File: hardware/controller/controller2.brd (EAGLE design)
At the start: 65.7 x 33.2 mm, 15 parts

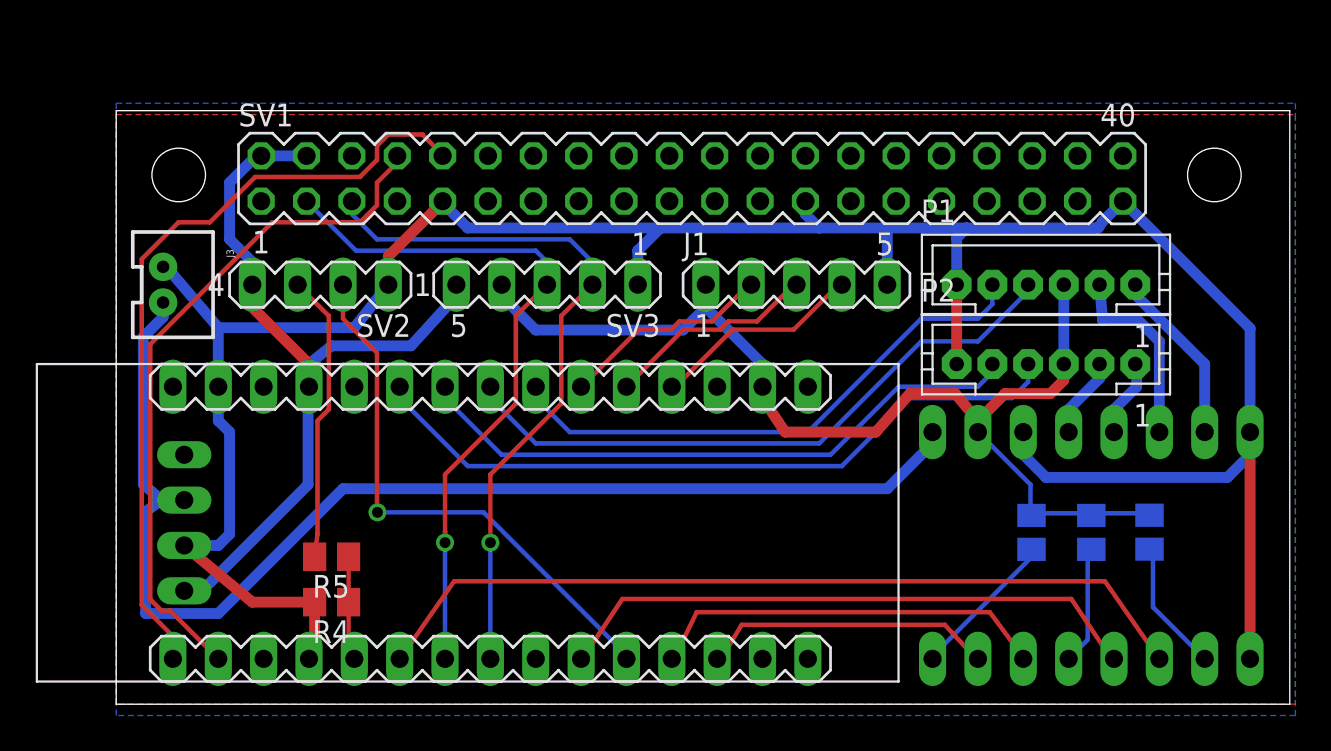
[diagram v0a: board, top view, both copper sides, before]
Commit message: auto ranging for rotary encoder, a few changes to the chassis, add rangefinder test
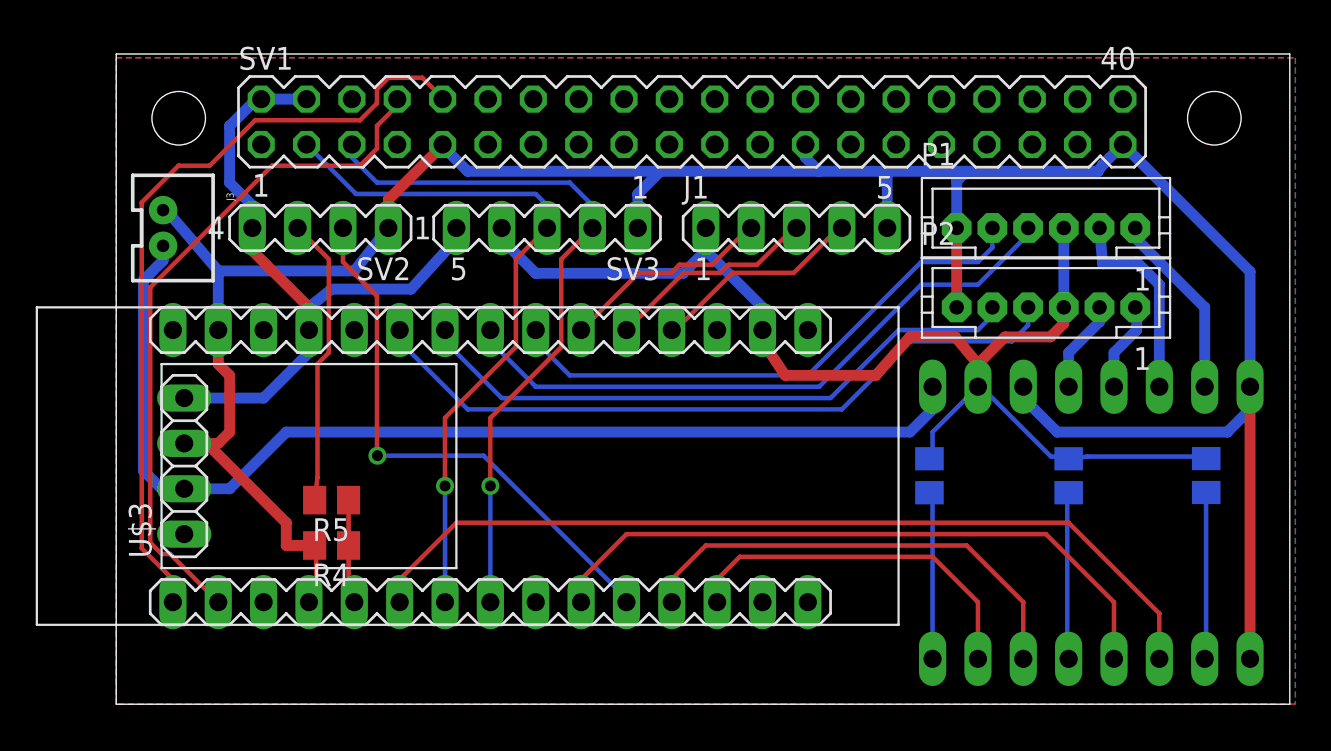
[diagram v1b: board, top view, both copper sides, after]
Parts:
- moved R1 6.54 mm to (45.5, 12.8)
- moved R2 4.49 mm to (61.0, 12.8)
- moved R3 3.42 mm to (53.3, 12.8)
- moved J1 3.18 mm to (38.1, 26.7)
- moved J3 3.18 mm to (3.17, 26.7)
- moved P1 3.18 mm to (52.1, 26.7)
- moved P2 3.18 mm to (52.1, 22.2)
- moved R4 3.18 mm to (12.1, 8.89)
- moved SV1 3.18 mm to (32.2, 32.6)
- moved SV2 3.18 mm to (11.4, 26.7)
- moved SV3 3.18 mm to (24.1, 26.7)
- moved U$1 3.18 mm to (21.0, 13.3)
- moved U$3 3.18 mm to (3.81, 13.3), flipped to the top, turned to 90 degrees
- moved R5 3.17 mm to (12.1, 11.4)
- moved U$2 1.27 mm to (54.6, 10.2)
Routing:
- net N$16: track 68.7 -> 60.8 mm
- net VCC: track 60.3 -> 67.9 mm
- net N$25: track 44.9 -> 39.3 mm
- net N$4: track 16.7 -> 20.6 mm
- net N$3: track 22.6 -> 26.2 mm
- net N$2: track 33.6 -> 36.9 mm
- net N$1: track 47.1 -> 49.8 mm
- net N$8: track 6.74 -> 9.38 mm
- net GND: track 148.5 -> 150.9 mm
- net N$6: track 7.49 -> 9.34 mm
- net N$7: track 8.43 -> 9.45 mm
- net N$11: track 9.87 -> 10.5 mm
- net N$9: track 4.37 -> 5.00 mm
- net N$10: track 10.8 -> 11.4 mm
- net N$5: track 4.53 -> 5.16 mm
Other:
- board size 65.7 x 33.2 mm -> 65.7 x 36.4 mm
